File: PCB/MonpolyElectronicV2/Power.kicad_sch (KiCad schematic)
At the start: 20 parts, among them J2 10155435-00011LF, U2 BQ25895RTWR, U3 TPS62162DSG

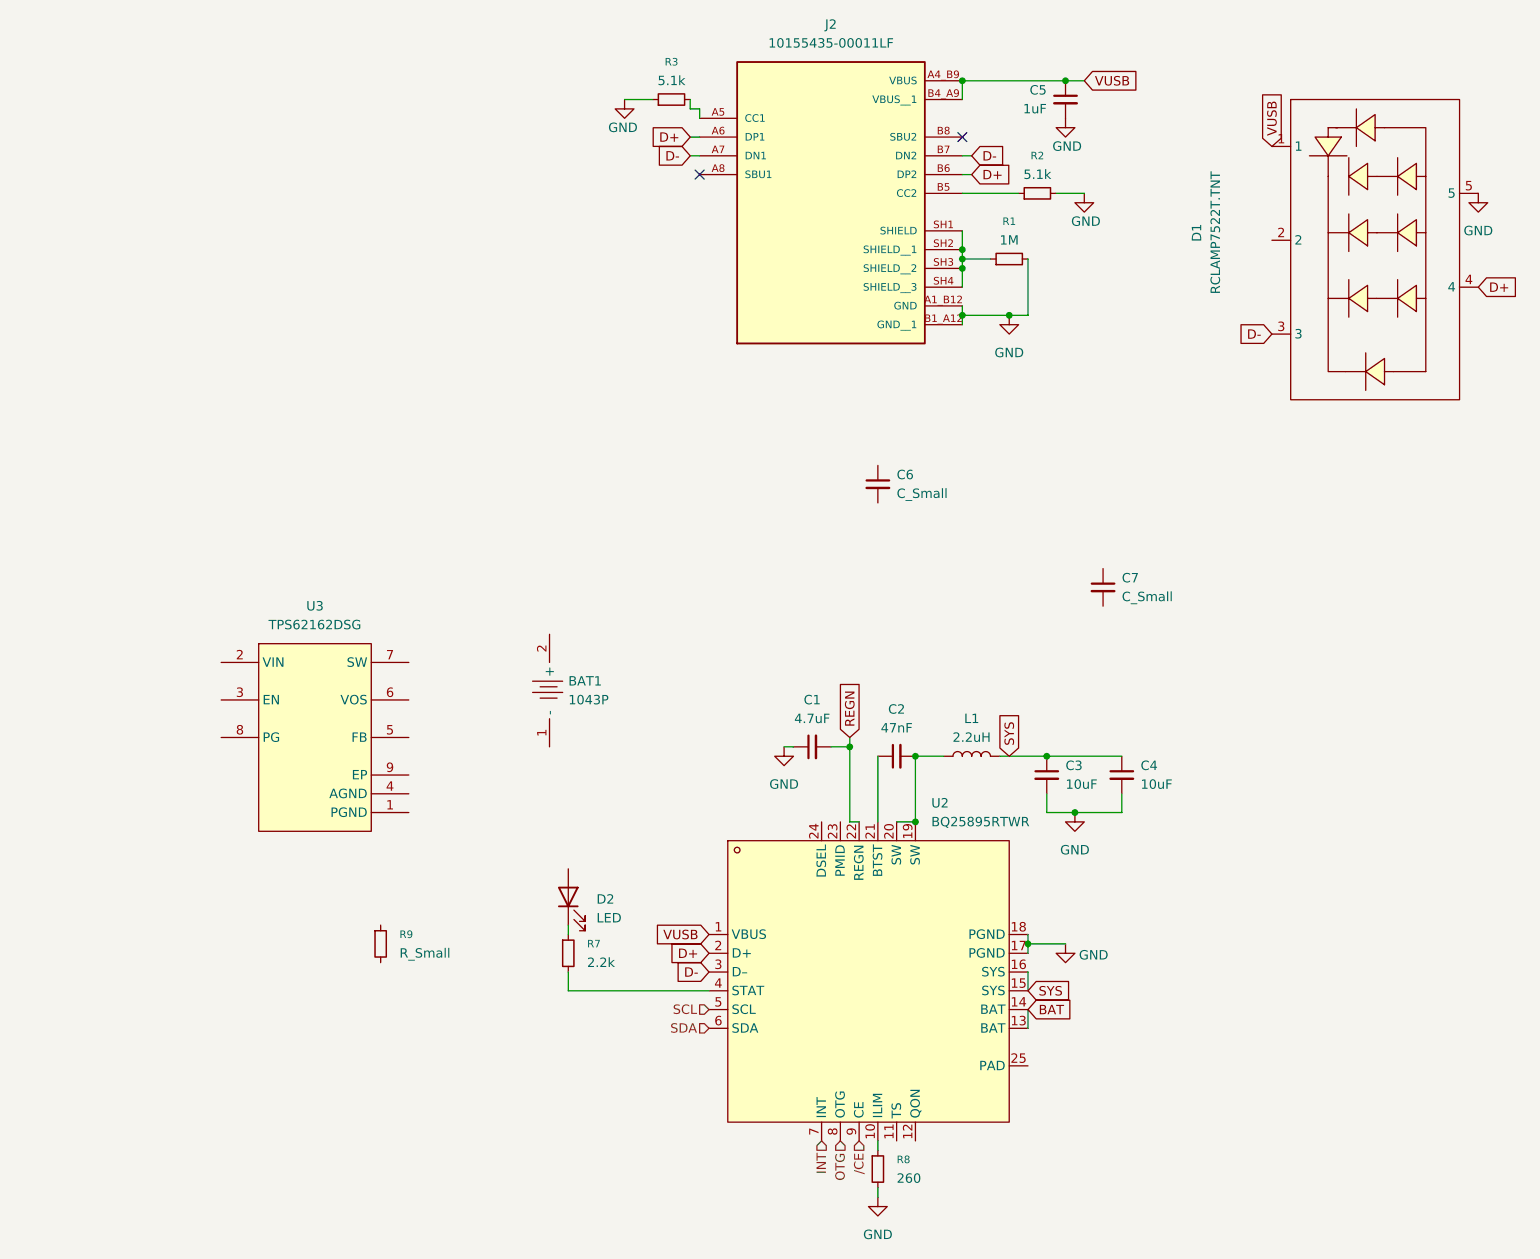
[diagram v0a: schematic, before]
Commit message: continue battery circuit. Finished BQ25895RTWR and USB wiring
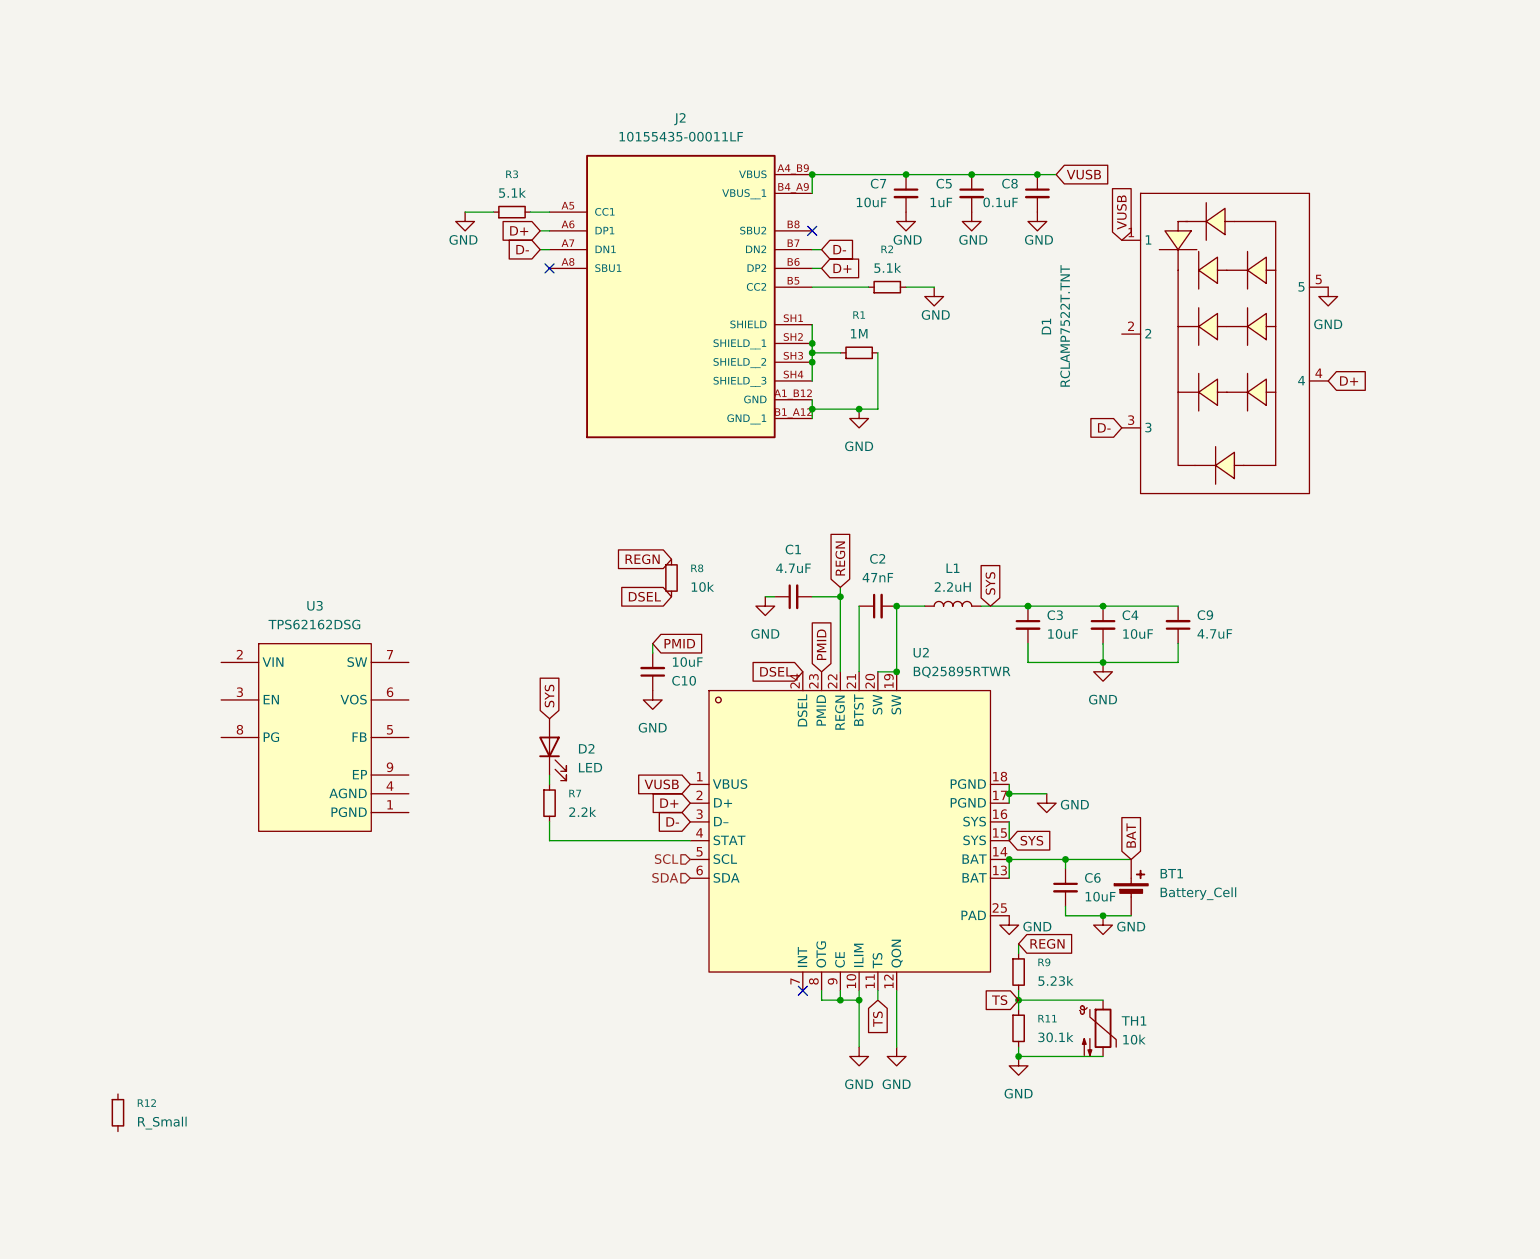
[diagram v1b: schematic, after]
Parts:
- removed BAT1: 1043P, easyeda2kicad:BAT-TH_1043P, symbol easyeda2kicad:1043P
- added BT1: Battery_Cell, easyeda2kicad:BAT-TH_1043P, symbol Device:Battery_Cell
- added C10: 10uF, symbol Device:C_Small
- added C8: 0.1uF, symbol Device:C_Small
- added C9: 4.7uF, symbol Device:C_Small
- added R11: 30.1k, symbol Device:R_Small
- added R12: R_Small, symbol Device:R_Small
- added TH1: 10k, symbol Device:Thermistor_NTC
- C6, C7: value C_Small -> 10uF
- R8: value 260 -> 10k
- R9: value R_Small -> 5.23k
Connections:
- net OTG is gone; now on net GND: U2.8 (OTG)
- net /CE is gone; now on net GND: U2.9 (CE)
- net BAT: now also C6.1, BT1.1 (+)
- net GND: now also C6.2, C7.2, U2.10 (ILIM), U2.12 (QON), U2.25 (PAD), BT1.2 (-), C10.1, C8.2, C9.1, R11.2, TH1.2; no longer R8.2
- net REGN: now also R8.1, R9.1
- net SYS: now also D2.2 (A), C9.2
- net VUSB: now also C7.1, C8.1
- net TS: now reaches U2.11 (TS)
- net TS: now also R9.2, R11.1, TH1.1
- net PMID: now reaches U2.23 (PMID)
- net PMID: now also C10.2
- net DSEL: now reaches U2.24 (DSEL)
- net DSEL: now also R8.2
- net INT: no longer names the net of U2.7 (INT)
- no-connect marks 2 -> 3
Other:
- moved on the sheet: C1, C2, C3, C4, C5, C6, D1, D2, J2, L1, R1, R2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

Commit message: work on Logic part (MCU): audio done, programming done, ESP32 and inputs WIP, diplay not yet started
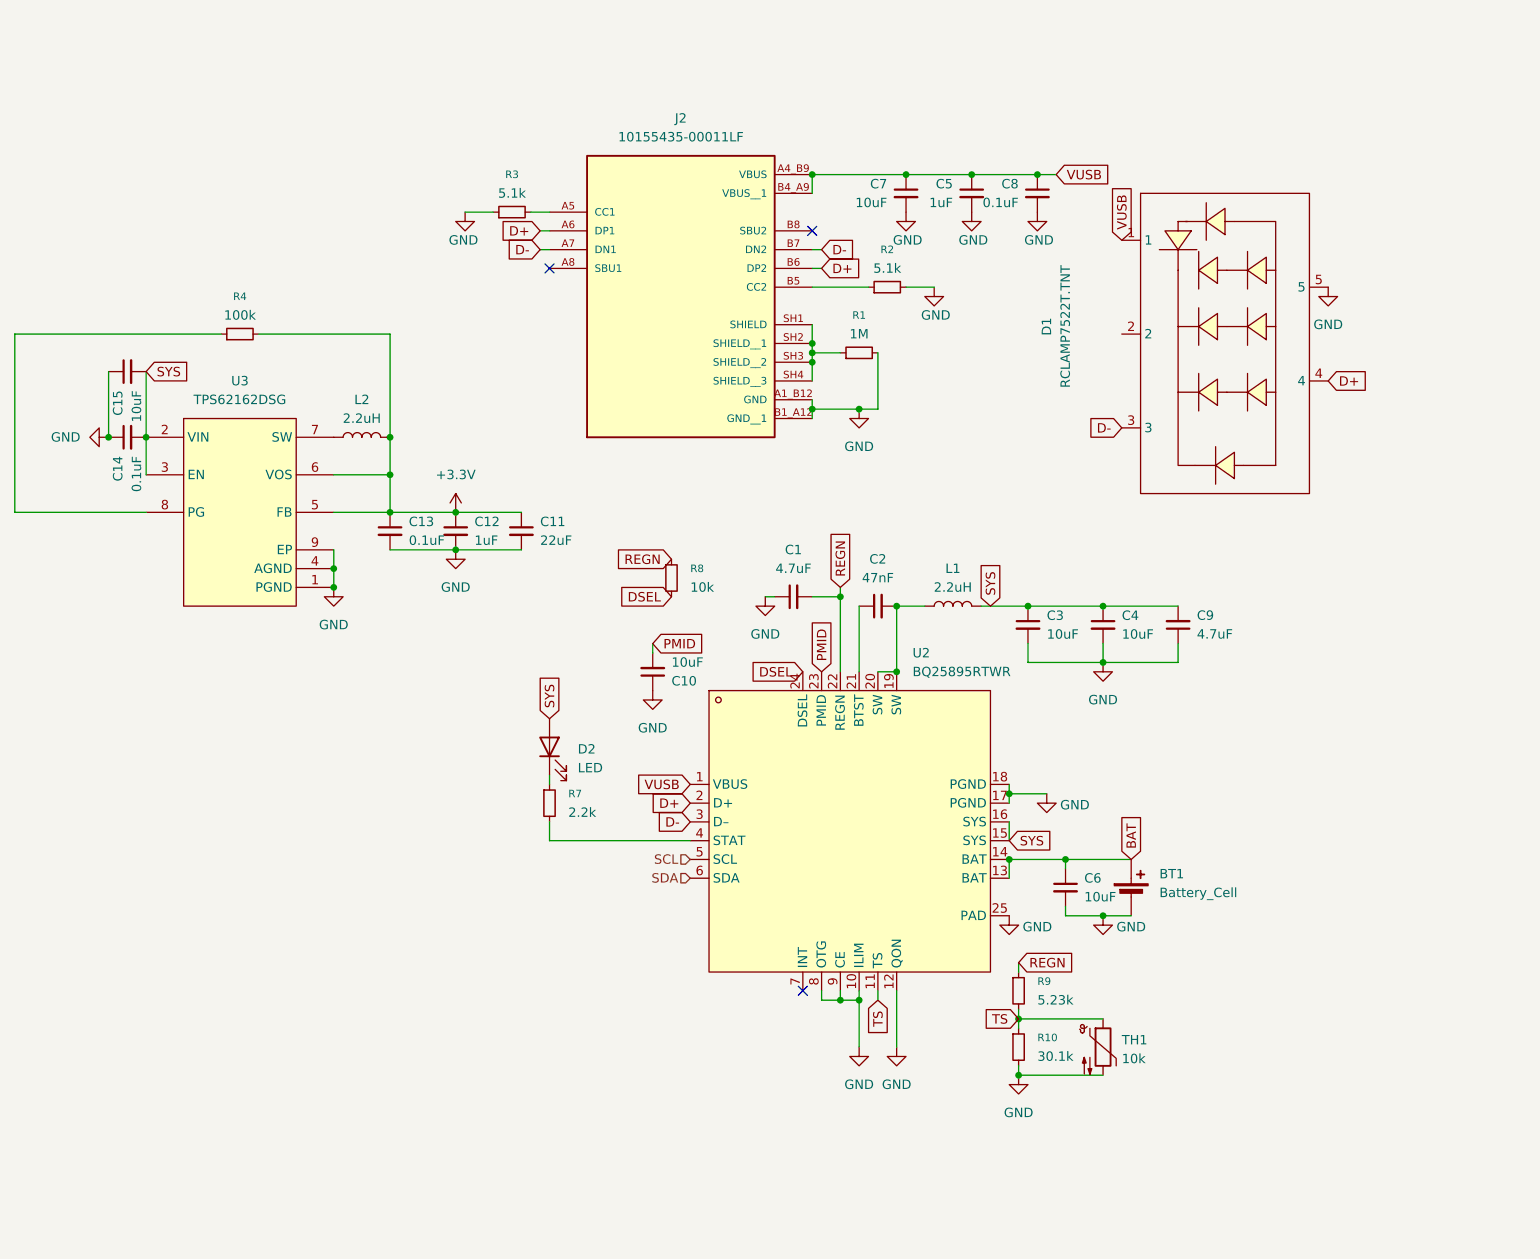
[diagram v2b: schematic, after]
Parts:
- removed R11: 30.1k, symbol Device:R_Small
- removed R12: R_Small, symbol Device:R_Small
- added C11: 22uF, symbol Device:C_Small
- added C12: 1uF, symbol Device:C_Small
- added C13, C14: 0.1uF, symbol Device:C_Small
- added C15: 10uF, symbol Device:C_Small
- added L2: 2.2uH, symbol Device:L
- added R10: 30.1k, symbol Device:R_Small
- added R4: 100k, symbol Device:R_Small
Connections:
- net GND: now also U3.1 (PGND), U3.4 (AGND), U3.9 (EP), C11.2, C12.2, C13.2, C14.1, C15.1, R10.2
- net SYS: now also U3.2 (VIN), U3.3 (EN), C14.2, C15.2
- net TS: now also R10.1
- net +3.3V: now reaches U3.5 (FB)
- net +3.3V: now also U3.6 (VOS), C11.1, C12.1, C13.1, L2.2, R4.2
- net at U3.7 (SW): now also L2.1
- net at U3.8 (PG): now also R4.1
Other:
- moved on the sheet: R9, TH1, U3

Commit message: Start adding footprints
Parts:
- C1, C12, C13, C14, C5, C8, C9: footprint (none) -> Capacitor_SMD:C_0603_1608Metric
- C10, C11, C15, C3, C4, C6, C7: footprint (none) -> Capacitor_SMD:C_0805_2012Metric
- L1: footprint (none) -> Extra:IND_SRP4020TA_BRN
- L2: footprint (none) -> Extra:WE-LQS_5040
- R2, R3: footprint 5.1k -> (none)
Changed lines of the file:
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@@
 			)
 		)
-		(property "Footprint" ""
+		(property "Footprint" "Capacitor_SMD:C_0805_2012Metric"
 			(at 139.7 54.61 0)
 			(effects
@@
 			)
 		)
-		(property "Footprint" ""
+		(property "Footprint" "Capacitor_SMD:C_0603_1608Metric"
 			(at 69.85 100.33 0)
 			(effects
@@
 			)
 		)
-		(property "Footprint" ""
+		(property "Footprint" "Capacitor_SMD:C_0603_1608Metric"
 			(at 148.59 54.61 0)
 			(effects
@@
 			)
 		)
-		(property "Footprint" ""
+		(property "Footprint" "Capacitor_SMD:C_0603_1608Metric"
 			(at 124.46 109.22 0)
 			(effects
@@
 			)
 		)
-		(property "Footprint" ""
+		(property "Footprint" "Capacitor_SMD:C_0805_2012Metric"
 			(at 161.29 148.59 0)
 			(effects
@@
 			)
 		)
-		(property "Footprint" ""
+		(property "Footprint" "Capacitor_SMD:C_0805_2012Metric"
 			(at 166.37 113.03 0)
 			(effects
@@
 			)
 		)
-		(property "Footprint" "5.1k"
+		(property "Footprint" ""
 			(at 137.16 67.31 0)
 			(effects
@@
 			)
 		)
-		(property "Footprint" ""
+		(property "Footprint" "Capacitor_SMD:C_0805_2012Metric"
 			(at 87.63 100.33 0)
 			(effects
@@
 			)
 		)
-		(property "Footprint" ""
+		(property "Footprint" "Extra:WE-LQS_5040"
 			(at 66.04 87.63 0)
 			(effects
@@
 			)
 		)
-		(property "Footprint" ""
+		(property "Footprint" "Capacitor_SMD:C_0805_2012Metric"
 			(at 156.21 113.03 0)
 			(effects
@@
 			)
 		)
-		(property "Footprint" ""
+		(property "Footprint" "Capacitor_SMD:C_0805_2012Metric"
 			(at 105.41 119.38 0)
 			(effects
@@
 			)
 		)
-		(property "Footprint" "5.1k"
+		(property "Footprint" ""
 			(at 86.36 57.15 0)
 			(effects
@@
 			)
 		)
-		(property "Footprint" ""
+		(property "Footprint" "Extra:IND_SRP4020TA_BRN"
 			(at 146.05 110.49 0)
 			(effects
@@
 			)
 		)
-		(property "Footprint" ""
+		(property "Footprint" "Capacitor_SMD:C_0805_2012Metric"
 			(at 34.29 78.74 0)
 			(effects
@@
 			)
 		)
-		(property "Footprint" ""
+		(property "Footprint" "Capacitor_SMD:C_0603_1608Metric"
 			(at 78.74 100.33 0)
 			(effects
@@
 			)
 		)
-		(property "Footprint" ""
+		(property "Footprint" "Capacitor_SMD:C_0603_1608Metric"
 			(at 157.48 54.61 0)
 			(effects
@@
 			)
 		)
-		(property "Footprint" ""
+		(property "Footprint" "Capacitor_SMD:C_0603_1608Metric"
 			(at 176.53 113.03 0)
 			(effects
@@
 			)
 		)
-		(property "Footprint" ""
+		(property "Footprint" "Capacitor_SMD:C_0603_1608Metric"
 			(at 34.29 87.63 0)
 			(effects

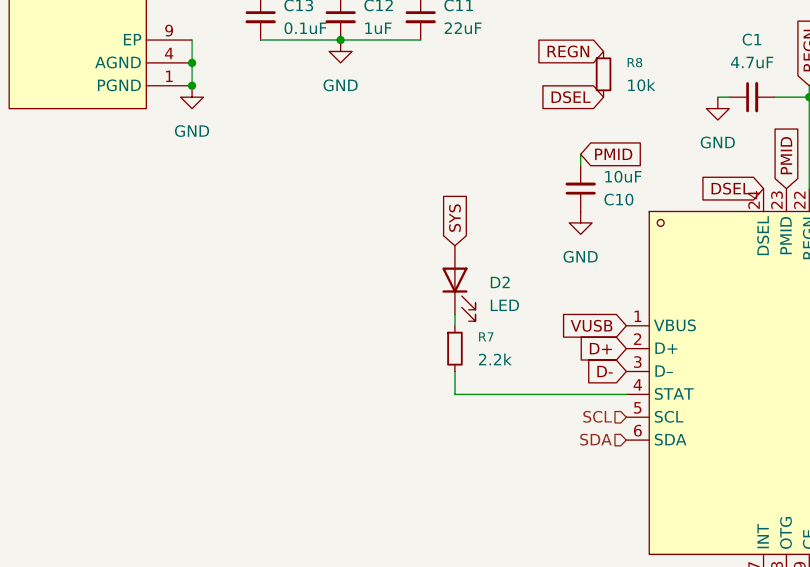
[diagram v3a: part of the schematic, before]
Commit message: add symbols + multiple backlight options
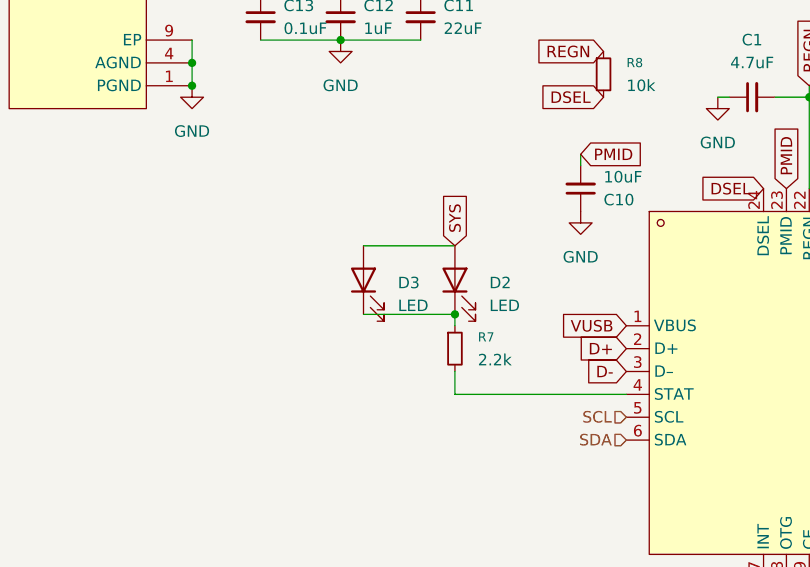
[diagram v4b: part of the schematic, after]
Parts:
- added D3: LED, LED_THT:LED_D5.0mm_Horizontal_O1.27mm_Z3.0mm, symbol Device:LED
- C2: footprint (none) -> Capacitor_SMD:C_0402_1005Metric
- D2: footprint (none) -> LED_SMD:LED_0603_1608Metric
- R1, R10, R2, R3, R4, R7, R8, R9, TH1: footprint (none) -> Resistor_SMD:R_0603_1608Metric
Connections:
- net SYS: now also D3.2 (A)
- net at D2.1 (K), R7.1: now also D3.1 (K)
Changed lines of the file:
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@@
 	)
 	(junction
+		(at 91.44 133.35)
+		(diameter 0)
+		(color 0 0 0 0)
+	)
+	(junction
 		(at 78.74 97.79)
 		(diameter 0)
@@
 	(wire
 		(pts
+			(xy 81.28 133.35) (xy 91.44 133.35)
+		)
+		(stroke
+			(width 0)
+			(type default)
+		)
+	)
+	(wire
+		(pts
 			(xy 69.85 97.79) (xy 78.74 97.79)
 		)
@@
 	(wire
 		(pts
+			(xy 81.28 125.73) (xy 91.44 125.73)
+		)
+		(stroke
+			(width 0)
+			(type default)
+		)
+	)
+	(wire
+		(pts
 			(xy 138.43 110.49) (xy 138.43 119.38)
 		)
@@
 			)
 		)
-		(property "Footprint" ""
+		(property "Footprint" "Resistor_SMD:R_0603_1608Metric"
 			(at 154.94 170.18 0)
 			(effects
@@
 	)
 	(symbol
+		(lib_id "Device:LED")
+		(at 81.28 129.54 90)
+		(unit 1)
+		(exclude_from_sim no)
+		(in_bom yes)
+		(on_board yes)
+		(dnp no)
+		(fields_autoplaced yes)
+		(property "Reference" "D3"
+			(at 85.09 129.8574 90)
+			(effects
+				(font
+					(size 1.27 1.27)
+				)
+				(justify right)
+			)
+		)
+		(property "Value" "LED"
+			(at 85.09 132.3974 90)
+			(effects
+				(font
+					(size 1.27 1.27)
+				)
+				(justify right)
+			)
+		)
+		(property "Footprint" "LED_THT:LED_D5.0mm_Horizontal_O1.27mm_Z3.0mm"
+			(at 81.28 129.54 0)
+			(effects
+				(font
+					(size 1.27 1.27)
+				)
+				(hide yes)
+			)
+		)
+		(property "Datasheet" "~"
+			(at 81.28 129.54 0)
+			(effects
+				(font
+					(size 1.27 1.27)
+				)
+				(hide yes)
+			)
+		)
+		(property "Description" "Light emitting diode"
+			(at 81.28 129.54 0)
+			(effects
+				(font
+					(size 1.27 1.27)
+				)
+				(hide yes)
+			)
+		)
+		(property "Sim.Pins" "1=K 2=A"
+			(at 81.28 129.54 0)
+			(effects
+				(font
+					(size 1.27 1.27)
+				)
+				(hide yes)
+			)
+		)
+		(pin "1"
+		)
+		(pin "2"
+		)
+		(instances
+			(project "MonpolyElectronicV2"
+				(path "/d7c31a86-0f1d-461f-96b3-0b094256e729/f3a0dc57-f483-416a-a0c7-91cb7e9a3802"
+					(reference "D3")
+					(unit 1)
+				)
+			)
+		)
+	)
+	(symbol
 		(lib_id "power:GND")
 		(at 196.85 67.31 0)
@@
 			)
 		)
-		(property "Footprint" ""
+		(property "Footprint" "Resistor_SMD:R_0603_1608Metric"
 			(at 49.53 73.66 0)
 			(effects
@@
 			)
 		)
-		(property "Footprint" ""
+		(property "Footprint" "Resistor_SMD:R_0603_1608Metric"
 			(at 137.16 67.31 0)
 			(effects
@@
 			)
 		)
-		(property "Footprint" ""
+		(property "Footprint" "Resistor_SMD:R_0603_1608Metric"
 			(at 133.35 76.2 0)
 			(effects
@@
 			)
 		)
-		(property "Footprint" ""
+		(property "Footprint" "Capacitor_SMD:C_0402_1005Metric"
 			(at 135.89 110.49 0)
 			(effects
@@
 			)
 		)
-		(property "Footprint" ""
+		(property "Footprint" "LED_SMD:LED_0603_1608Metric"
 			(at 91.44 129.54 0)
 			(effects
@@
 			)
 		)
-		(property "Footprint" ""
+		(property "Footprint" "Resistor_SMD:R_0603_1608Metric"
 			(at 166.37 168.91 0)
 			(effects
@@
 			)
 		)
-		(property "Footprint" ""
+		(property "Footprint" "Resistor_SMD:R_0603_1608Metric"
 			(at 91.44 137.16 0)
 			(effects
@@
 			)
 		)
-		(property "Footprint" ""
+		(property "Footprint" "Resistor_SMD:R_0603_1608Metric"
 			(at 86.36 57.15 0)
 			(effects
@@
 			)
 		)
-		(property "Footprint" ""
+		(property "Footprint" "Resistor_SMD:R_0603_1608Metric"
 			(at 107.95 106.68 0)
 			(effects
@@
 			)
 		)
-		(property "Footprint" ""
+		(property "Footprint" "Resistor_SMD:R_0603_1608Metric"
 			(at 154.94 162.56 0)
 			(effects
